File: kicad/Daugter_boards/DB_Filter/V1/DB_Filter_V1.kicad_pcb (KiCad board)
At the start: 2 copper layers, 20.3 x 50.8 mm, 5 parts, among them P1 CONN_01X19, P2 CONN_01X19

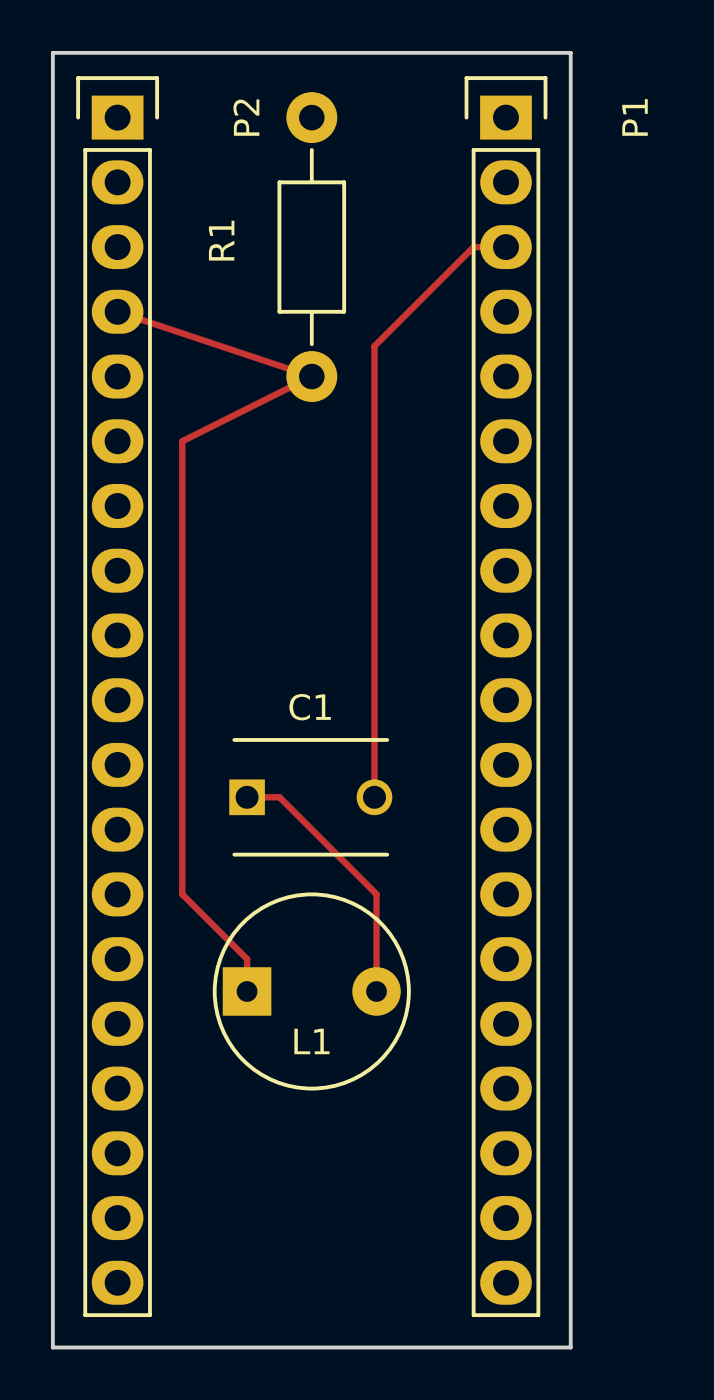
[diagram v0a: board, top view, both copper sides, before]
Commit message: update echopen footprint librairy for better finish
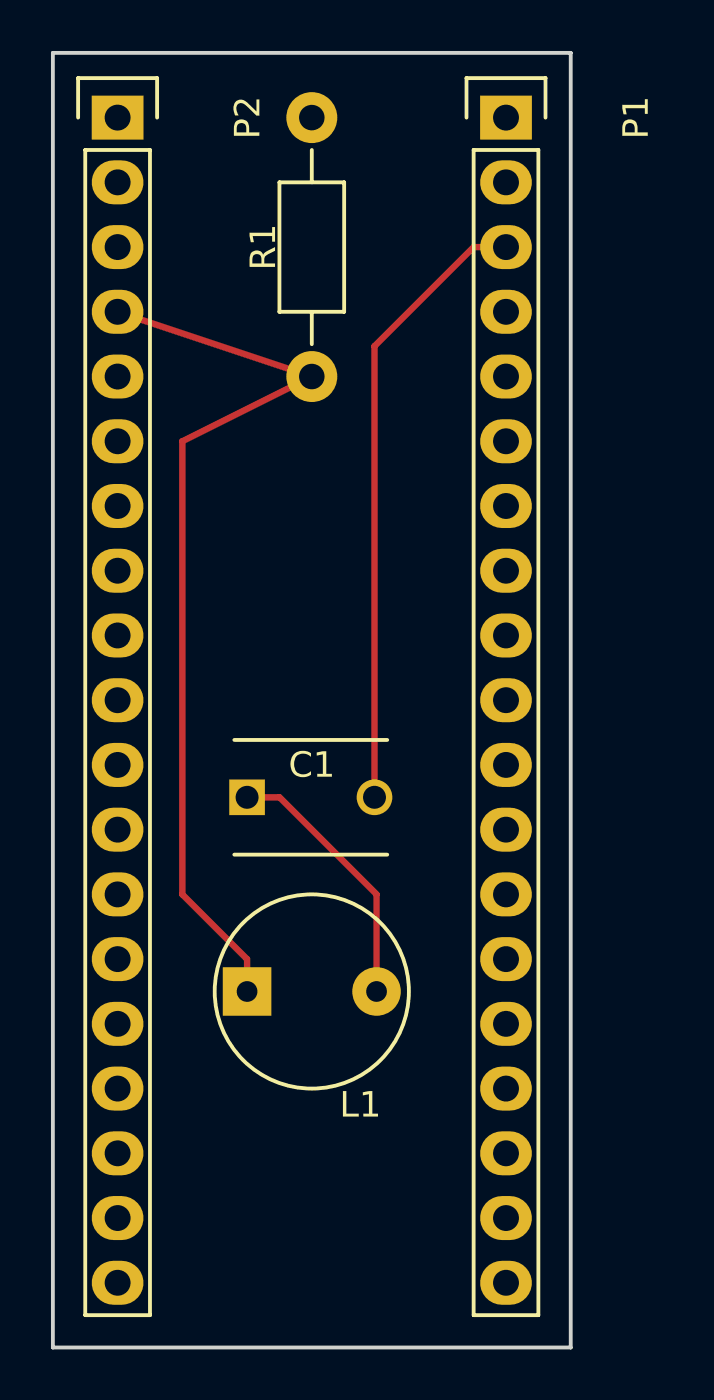
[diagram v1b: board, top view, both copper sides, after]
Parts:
- C1: footprint Capacitors_ThroughHole:C_Disc_D6_P5 -> echopen:C_TH_common
- L1: footprint Inductors:INDUCTOR_V -> echopen:INDUCTOR_TH_common
- R1: footprint Resistors_ThroughHole:Resistor_Horizontal_RM10mm -> echopen:Resistor_TH_common
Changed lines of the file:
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@@
     (add_net "Net-(P2-Pad9)")
-  )
-  (module Capacitors_ThroughHole:C_Disc_D6_P5 placed (layer F.Cu)
-    (at 90.17 90.17)
-    (descr "Capacitor 6mm Disc, Pitch 5mm")
-    (tags Capacitor)
-    (fp_text reference C1 (at 2.5 -3.5) (layer F.SilkS)
-      (effects (font (size 1 1) (thickness 0.15)))
-    )
-    (fp_text value 1000p (at 2.5 3.5) (layer F.Fab)
-      (effects (font (size 1 1) (thickness 0.15)))
-    )
-    (fp_line (start -0.95 -2.5) (end 5.95 -2.5) (layer F.CrtYd) (width 0.05))
-    (fp_line (start 5.95 -2.5) (end 5.95 2.5) (layer F.CrtYd) (width 0.05))
-    (fp_line (start 5.95 2.5) (end -0.95 2.5) (layer F.CrtYd) (width 0.05))
-    (fp_line (start -0.95 2.5) (end -0.95 -2.5) (layer F.CrtYd) (width 0.05))
-    (fp_line (start -0.5 -2.25) (end 5.5 -2.25) (layer F.SilkS) (width 0.15))
-    (fp_line (start 5.5 2.25) (end -0.5 2.25) (layer F.SilkS) (width 0.15))
-    (pad 1 thru_hole rect (at 0 0) (size 1.4 1.4) (drill 0.9) (layers *.Cu *.Mask F.SilkS)
-      (net 1 "Net-(C1-Pad1)"))
-    (pad 2 thru_hole circle (at 5 0) (size 1.4 1.4) (drill 0.9) (layers *.Cu *.Mask F.SilkS)
-      (net 2 "Net-(C1-Pad2)"))
-    (model Capacitors_ThroughHole.3dshapes/C_Disc_D6_P5.wrl
-      (at (xyz 0.0984252 0 0))
-      (scale (xyz 1 1 1))
-      (rotate (xyz 0 0 0))
-    )
-  )
-  (module Inductors:INDUCTOR_V placed (layer F.Cu)
-    (at 92.71 97.79)
-    (descr "Inductor (vertical)")
-    (tags INDUCTOR)
-    (fp_text reference L1 (at 0 1.99898) (layer F.SilkS)
-      (effects (font (size 1 1) (thickness 0.15)))
-    )
-    (fp_text value 10u (at 0.09906 -1.99898) (layer F.Fab)
-      (effects (font (size 1 1) (thickness 0.15)))
-    )
-    (fp_circle (center 0 0) (end 3.81 0) (layer F.SilkS) (width 0.15))
-    (pad 1 thru_hole rect (at -2.54 0) (size 1.905 1.905) (drill 0.8128) (layers *.Cu *.Mask F.SilkS)
-      (net 3 "Net-(L1-Pad1)"))
-    (pad 2 thru_hole circle (at 2.54 0) (size 1.905 1.905) (drill 0.8128) (layers *.Cu *.Mask F.SilkS)
-      (net 1 "Net-(C1-Pad1)"))
-    (model Inductors.3dshapes/INDUCTOR_V.wrl
-      (at (xyz 0 0 0))
-      (scale (xyz 2 2 2))
-      (rotate (xyz 0 0 0))
-    )
   )
   (module Socket_Strips:Socket_Strip_Straight_1x19 placed (layer F.Cu)
@@
     )
   )
-  (module Resistors_ThroughHole:Resistor_Horizontal_RM10mm (layer F.Cu)
+  (module echopen:Resistor_TH_common (layer F.Cu)
     (at 92.71 73.66 90)
     (descr "Resistor, Axial,  RM 10mm, 1/3W")
     (tags "Resistor Axial RM 10mm 1/3W")
-    (fp_text reference R1 (at 5.32892 -3.50012 90) (layer F.SilkS)
-      (effects (font (size 1 1) (thickness 0.15)))
-    )
-    (fp_text value 330 (at 5.08 3.81 90) (layer F.Fab)
+    (fp_text reference R1 (at 5.08 -1.905 90) (layer F.SilkS)
+      (effects (font (size 1 1) (thickness 0.15)))
+    )
+    (fp_text value 330 (at 5.08 1.905 90) (layer F.Fab)
       (effects (font (size 1 1) (thickness 0.15)))
     )
@@
       (rotate (xyz 0 0 0))
     )
+  )
+  (module echopen:C_TH_common (layer F.Cu)
+    (at 90.17 90.17)
+    (descr "Capacitor 6mm Disc, Pitch 5mm")
+    (tags Capacitor)
+    (fp_text reference C1 (at 2.54 -1.27) (layer F.SilkS)
+      (effects (font (size 1 1) (thickness 0.15)))
+    )
+    (fp_text value 1000p (at 2.54 1.27) (layer F.Fab)
+      (effects (font (size 1 1) (thickness 0.15)))
+    )
+    (fp_line (start -0.95 -2.5) (end 5.95 -2.5) (layer F.CrtYd) (width 0.05))
+    (fp_line (start 5.95 -2.5) (end 5.95 2.5) (layer F.CrtYd) (width 0.05))
+    (fp_line (start 5.95 2.5) (end -0.95 2.5) (layer F.CrtYd) (width 0.05))
+    (fp_line (start -0.95 2.5) (end -0.95 -2.5) (layer F.CrtYd) (width 0.05))
+    (fp_line (start -0.5 -2.25) (end 5.5 -2.25) (layer F.SilkS) (width 0.15))
+    (fp_line (start 5.5 2.25) (end -0.5 2.25) (layer F.SilkS) (width 0.15))
+    (pad 1 thru_hole rect (at 0 0) (size 1.4 1.4) (drill 0.9) (layers *.Cu *.Mask F.SilkS)
+      (net 1 "Net-(C1-Pad1)"))
+    (pad 2 thru_hole circle (at 5 0) (size 1.4 1.4) (drill 0.9) (layers *.Cu *.Mask F.SilkS)
+      (net 2 "Net-(C1-Pad2)"))
+    (model Capacitors_ThroughHole.3dshapes/C_Disc_D6_P5.wrl
+      (at (xyz 0.098425 0 0))
+      (scale (xyz 1 1 1))
+      (rotate (xyz 0 0 0))
+    )
+  )
+  (module echopen:INDUCTOR_TH_common (layer F.Cu)
+    (at 92.71 97.79)
+    (descr "Inductor (vertical)")
+    (tags INDUCTOR)
+    (fp_text reference L1 (at 1.905 4.445) (layer F.SilkS)
+      (effects (font (size 1 1) (thickness 0.15)))
+    )
+    (fp_text value 10u (at 0.09906 -1.99898) (layer F.Fab)
+      (effects (font (size 1 1) (thickness 0.15)))
+    )
+    (fp_circle (center 0 0) (end 3.81 0) (layer F.SilkS) (width 0.15))
+    (pad 1 thru_hole rect (at -2.54 0) (size 1.905 1.905) (drill 0.8128) (layers *.Cu *.Mask F.SilkS)
+      (net 3 "Net-(L1-Pad1)"))
+    (pad 2 thru_hole circle (at 2.54 0) (size 1.905 1.905) (drill 0.8128) (layers *.Cu *.Mask F.SilkS)
+      (net 1 "Net-(C1-Pad1)"))
+    (model Inductors.3dshapes/INDUCTOR_V.wrl
+      (at (xyz 0 0 0))
+      (scale (xyz 2 2 2))
+      (rotate (xyz 0 0 0))
+    )
